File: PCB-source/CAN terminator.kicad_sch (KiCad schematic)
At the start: 9 parts, among them Q2 AO3400A, Q3 AO3400A, Q5 AO3400A, Q6 AO3400A, SW5 SW_DIP_x02

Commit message: ch32
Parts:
- removed SW5: SW_DIP_x02, Button_Switch_SMD:SW_DIP_SPSTx02_Slide_6.7x6.64mm_W8.61mm_P2.54mm_LowProfile, symbol Switch:SW_DIP_x02
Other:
- moved on the sheet: Q2, Q3, R1, R5

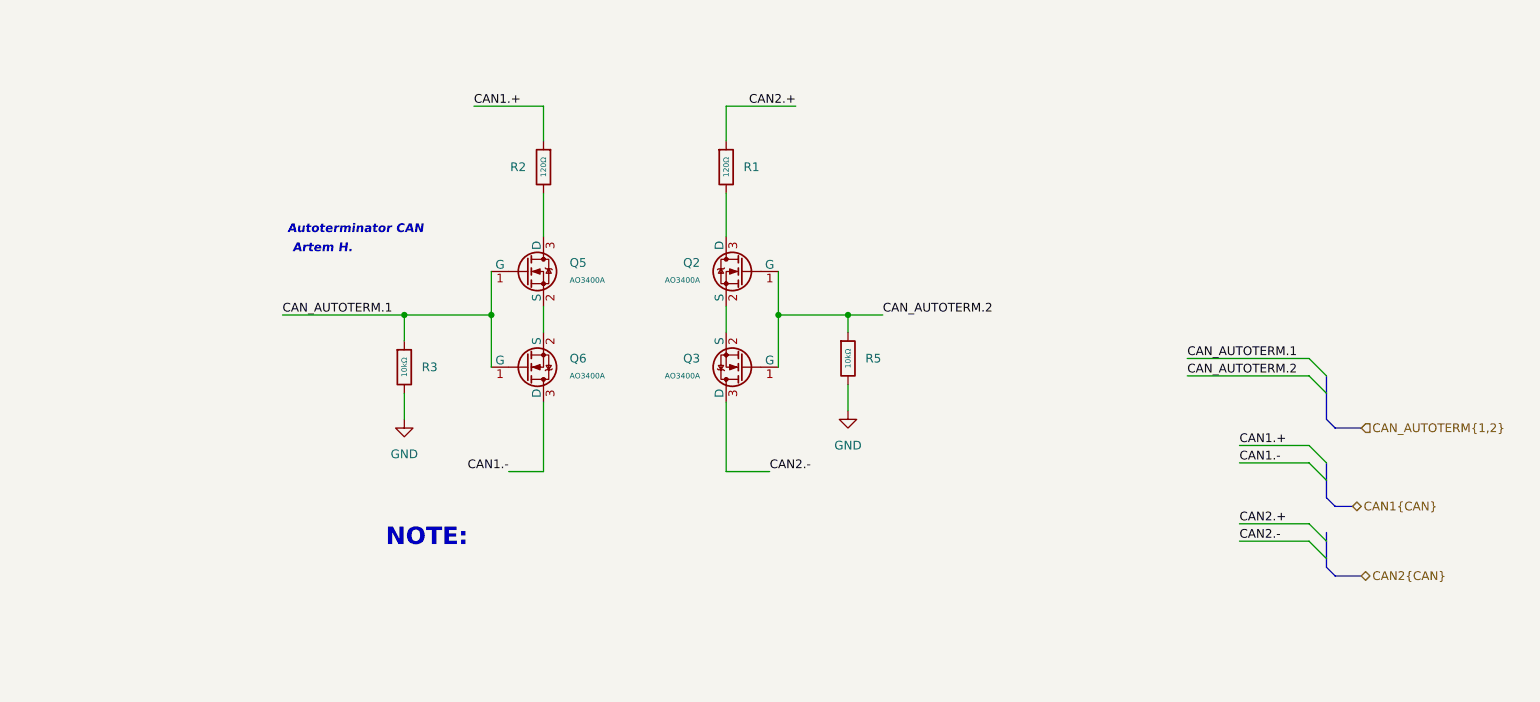
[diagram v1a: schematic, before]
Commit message: change can term add usr led
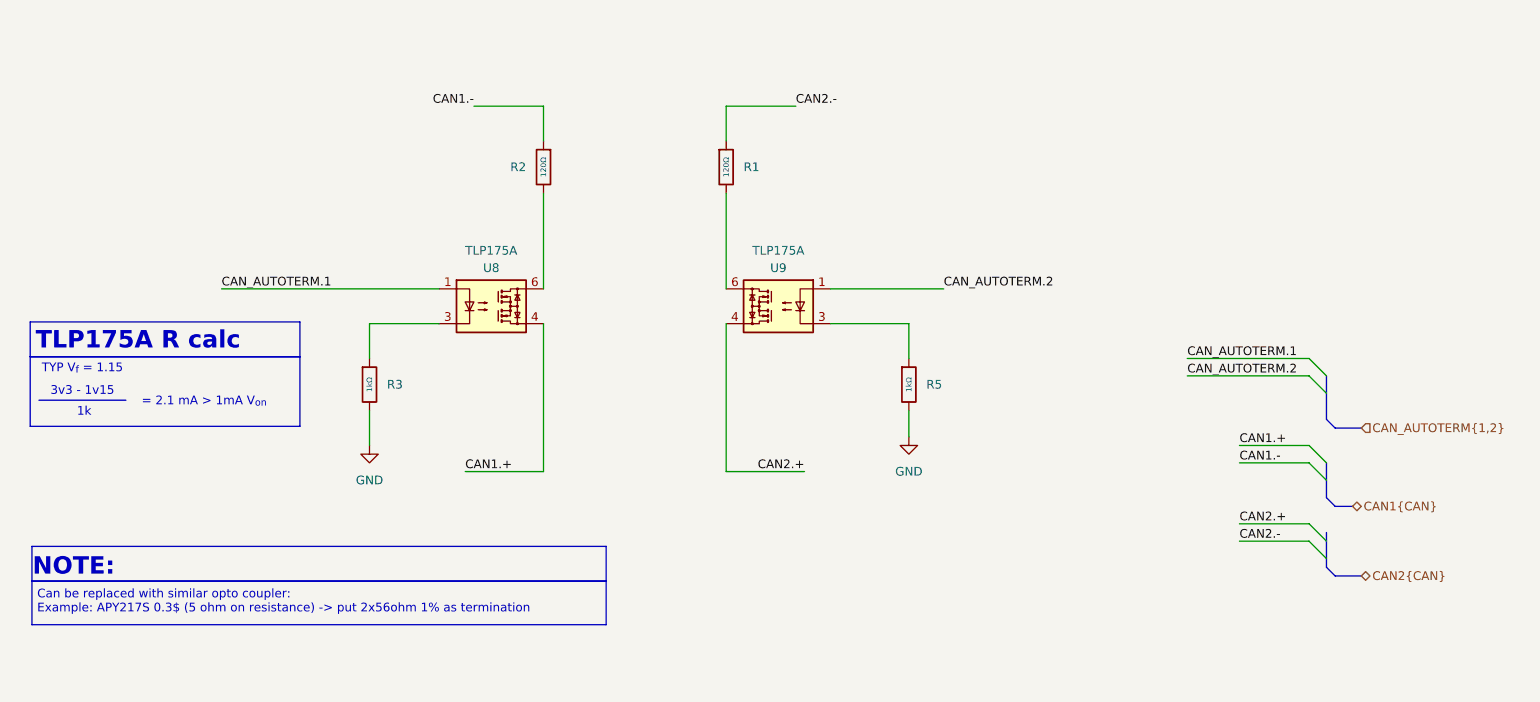
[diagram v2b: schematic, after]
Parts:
- removed Q2, Q3, Q5, Q6: AO3400A, PCM_JLCPCB:Q_SOT-23, symbol PCM_JLCPCB-Transistors:NMOS,AO3400A
- removed R3, R5: 10kΩ, PCM_JLCPCB:R_0402, symbol PCM_JLCPCB-Resistors:0402,10kΩ
- added R3, R5: 1kΩ, PCM_JLCPCB:R_0402, symbol PCM_JLCPCB-Resistors:0402,1kΩ
- added U8, U9: TLP175A, Package_SO:Toshiba_SOIC-4-6_4.4x3.6mm_P1.27mm, symbol Relay_SolidState:TLP175A
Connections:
- net CAN1.+: now also U8.4; no longer R2.1
- net CAN1.-: now also R2.1
- net CAN2.+: now also U9.4; no longer R1.1
- net CAN2.-: now also R1.1
- net CAN_AUTOTERM.1: now also U8.1
- net CAN_AUTOTERM.2: now also U9.1
- net GND: now also R3.2, R5.2
- net at R2.2: now also U8.6
- net at R1.2: now also U9.6
- new net: R3.1, U8.3
- new net: R5.1, U9.3
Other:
- note added: "1k"
- note added: "3v3 - 1v15"
- note added: "= 2.1 mA > 1mA V_{on}"
- note added: "Can be replaced with similar opto coupler: Example: APY217S 0.3$ (5 ohm on resistance) -> put 2x56ohm 1% as termination"
- note added: "TLP175A R calc"
- note added: "TYP V_{f} = 1.15"
- note removed: "Artem H."
- note removed: "Autoterminator CAN"

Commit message: bom done
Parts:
- U8, U9: LCSC (none) -> C141522
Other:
- note added: "Drop in chineese replacement part: GAQY221S, APY221S Same RDS-on. Turn on time -> dont care PIN COMPATIBLE"
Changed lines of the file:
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@@
+		)
+	)
+	(text "Drop in chineese replacement part:\nGAQY221S, APY221S\nSame RDS-on. Turn on time -> dont care\nPIN COMPATIBLE"
+		(exclude_from_sim no)
+		(at 44.196 148.082 0)
+		(effects
+			(font
+				(size 1.27 1.27)
+			)
+			(justify left)
 		)
 	)
@@
 		)
 		(property "Description" "MOSFET Photorelay 1-Form-A, Voff 60V, Ion 100mA, SOIC-4-6 (MFSOP-4-6)"
+			(at 110.49 96.52 0)
+			(effects
+				(font
+					(size 1.27 1.27)
+				)
+				(hide yes)
+			)
+		)
+		(property "LCSC" "C141522"
 			(at 110.49 96.52 0)
 			(effects
@@
 			(at 152.4 96.52 0)
 			(effects
+				(font
+					(size 1.27 1.27)
+				)
+				(hide yes)
+			)
+		)
+		(property "LCSC" "C141522"
+			(at 152.4 96.52 0)
+			(effects
